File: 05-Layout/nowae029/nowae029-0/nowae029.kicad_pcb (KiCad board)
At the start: 2 copper layers, 100 x 99.9 mm, 144 parts, among them P101 COMM_3, P102 SUPPLY_3, P103 COMM_4, P104 SUPPLY_4, P201 DEBUG, P401 BATTERY, P501 632722110112, U201 STM32L073CBT6, U301 TCA9554PWR, U302 TCA9554PWR, U401 TLV70233DBV, U501 FT230XS, U601 TCA9554PWR, U602 TCA9554PWR, Y201 32768

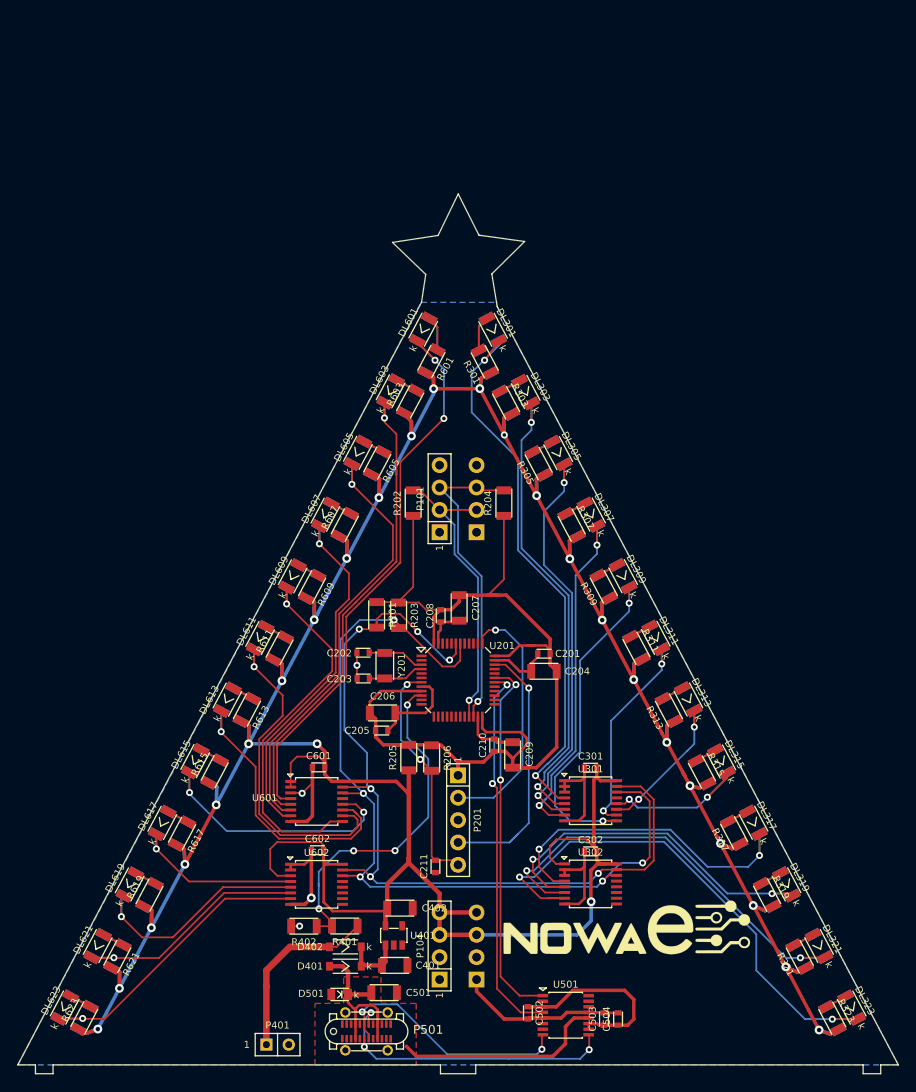
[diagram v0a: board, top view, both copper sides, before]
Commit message: WiP PCB TODO: resistors value into star page
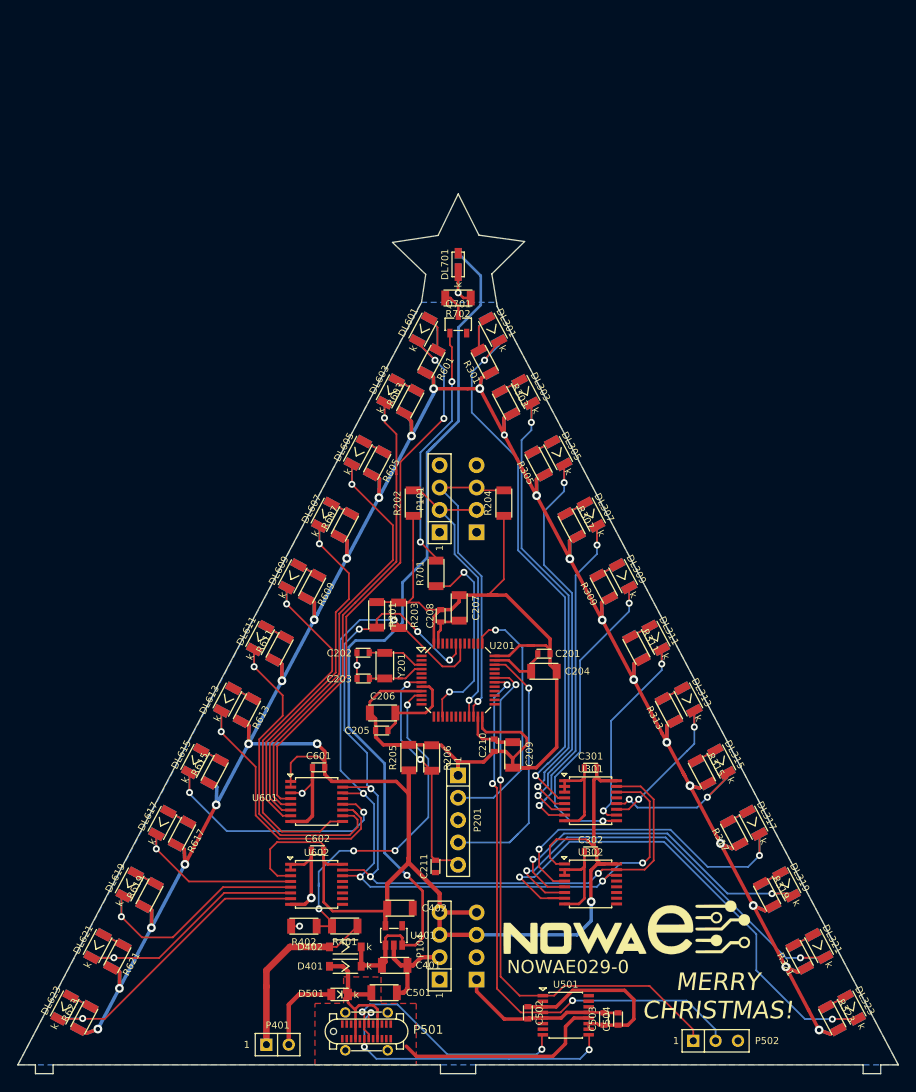
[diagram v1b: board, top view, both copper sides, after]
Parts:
- added DL701: WHITE, LEDs:LED-WURTH-WL_SWTP_3014, F.Cu at (100.0, 58.1)
- added DL702: WHITE, LEDs:LED-WURTH-WL_SWTP_3014, B.Cu at (100.0, 58.1)
- added P502: UART, CONNECTOR:CONN-STRIP-3x1-2.54, F.Cu at (129.2, 146.3)
- added Q701: BCW68GLT1G, SOT:SOT23-3, F.Cu at (100.0, 64.9)
- added R701: RESISTOR, RESISTOR:RESISTOR-1206, F.Cu at (97.5, 93.2)
- added R702: RESISTOR, RESISTOR:RESISTOR-1206, F.Cu at (100.0, 61.9)
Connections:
- net Net-(C401-Pad1) renamed +VDD
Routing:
- net +VDD: track 7.06 -> 104.9 mm, vias 0 -> 1
- net Net-(Q701-Pad1): track 0.00 -> 28.2 mm, vias 0 -> 2
- net /Microcontroller/STAR: track 0.00 -> 23.1 mm, vias 0 -> 2
- net /Communication/COMM_RX: track 43.8 -> 66.6 mm, vias 2 -> 3
- net GND: track 98.4 -> 119.7 mm
- net /Communication/COMM_TX: track 42.3 -> 63.2 mm
- net Net-(DL701-Pad1): track 0.00 -> 6.36 mm, vias 0 -> 1
- net Net-(Q701-Pad3): track 0.00 -> 2.94 mm
- net /Microcontroller/VDD_MCU: track 119.8 -> 120.4 mm
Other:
- board text added: "MERRY CHRISTMAS!"
- board text added: "NOWAE029-0"

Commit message: WiP: GND connections
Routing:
- net GND: track 119.7 -> 142.5 mm, vias 4 -> 13
- net +VDD: track 104.9 -> 101.9 mm
- net +VUSB: track 44.4 -> 47.0 mm
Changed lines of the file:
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@@
     (thickness 1.6)
     (drawings 57)
-    (tracks 1089)
+    (tracks 1128)
     (zones 0)
     (modules 150)
@@
   )
   (setup
-    (last_trace_width 0.2)
+    (last_trace_width 0.3)
     (user_trace_width 0.2)
     (user_trace_width 0.3)
@@
   (segment (start 108.3 104.3) (end 107.95 104.3) (width 0.3) (layer F.Cu) (net 2))
   (segment (start 105.75 103.05) (end 104.15 103.05) (width 0.3) (layer F.Cu) (net 2))
-  (segment (start 107 104.3) (end 105.75 103.05) (width 0.3) (layer F.Cu) (net 2))
   (segment (start 108.3 104.3) (end 108.3 103.41) (width 0.3) (layer F.Cu) (net 2))
   (segment (start 109.05 102.66) (end 109.05 102.3) (width 0.3) (layer F.Cu) (net 2))
-  (segment (start 108.3 103.41) (end 109.05 102.66) (width 0.3) (layer F.Cu) (net 2))
   (segment (start 99.97 98.7) (end 100.12 98.55) (width 0.3) (layer F.Cu) (net 2))
-  (segment (start 98.02 98.7) (end 99.97 98.7) (width 0.3) (layer F.Cu) (net 2))
   (segment (start 97.87 98.85) (end 98.02 98.7) (width 0.3) (layer F.Cu) (net 2))
   (segment (start 97.75 101.15) (end 97.75 99.88) (width 0.3) (layer F.Cu) (net 2))
@@
   (segment (start 96.314998 109.03) (end 92.88 109.03) (width 0.3) (layer F.Cu) (net 2))
   (segment (start 96.725 106.05) (end 97.09 106.415) (width 0.3) (layer F.Cu) (net 2))
-  (segment (start 97.09 106.415) (end 97.09 108.254998) (width 0.3) (layer F.Cu) (net 2))
   (segment (start 95.85 106.05) (end 96.725 106.05) (width 0.3) (layer F.Cu) (net 2))
   (segment (start 107 104.3) (end 108.3 104.3) (width 0.3) (layer F.Cu) (net 2))
@@
   (segment (start 95.818 136.77) (end 97.9 136.77) (width 0.5) (layer F.Cu) (net 2))
   (segment (start 94.888 137.7) (end 95.818 136.77) (width 0.5) (layer F.Cu) (net 2))
-  (segment (start 94.25 137.7) (end 94.25 140.37) (width 0.5) (layer F.Cu) (net 2))
   (segment (start 93.82 140.8) (end 93.05 140.8) (width 0.5) (layer F.Cu) (net 2))
   (segment (start 94.25 140.37) (end 93.82 140.8) (width 0.5) (layer F.Cu) (net 2))
@@
   (segment (start 80.77 142.166) (end 80.77 146.7) (width 0.5) (layer F.Cu) (net 2))
   (segment (start 81.936 141) (end 80.77 142.166) (width 0.5) (layer F.Cu) (net 2))
+  (segment (start 86.85 143.4) (end 87.2 143.05) (width 0.3) (layer F.Cu) (net 2))
+  (segment (start 86.85 144.37) (end 86.85 143.4) (width 0.3) (layer F.Cu) (net 2))
+  (segment (start 86.85 147) (end 87.2 147.35) (width 0.3) (layer F.Cu) (net 2))
+  (segment (start 86.85 146.03) (end 86.85 147) (width 0.3) (layer F.Cu) (net 2))
+  (segment (start 92.35 147) (end 92 147.35) (width 0.3) (layer F.Cu) (net 2))
+  (segment (start 92.35 146.03) (end 92.35 147) (width 0.3) (layer F.Cu) (net 2))
+  (segment (start 92.35 143.4) (end 92 143.05) (width 0.3) (layer F.Cu) (net 2))
+  (segment (start 92.35 144.37) (end 92.35 143.4) (width 0.3) (layer F.Cu) (net 2))
+  (via (at 94.25 139.35) (size 1) (drill 0.5) (layers F.Cu B.Cu) (net 2))
+  (segment (start 94.25 137.7) (end 94.25 139.35) (width 0.5) (layer F.Cu) (net 2))
+  (segment (start 94.25 139.35) (end 94.25 140.37) (width 0.5) (layer F.Cu) (net 2))
+  (segment (start 92.35 144.37) (end 92.35 146.03) (width 0.3) (layer F.Cu) (net 2))
+  (segment (start 86.85 144.37) (end 86.85 146.03) (width 0.3) (layer F.Cu) (net 2))
+  (segment (start 97.43 127.16) (end 96.88 127.16) (width 0.2) (layer F.Cu) (net 2))
+  (via (at 96.04 124.61) (size 0.8) (drill 0.4) (layers F.Cu B.Cu) (net 2))
+  (segment (start 96.04 126.32) (end 96.04 124.61) (width 0.2) (layer F.Cu) (net 2))
+  (segment (start 96.88 127.16) (end 96.04 126.32) (width 0.2) (layer F.Cu) (net 2))
+  (segment (start 94.85 135.802) (end 95.818 136.77) (width 0.4) (layer F.Cu) (net 2))
+  (segment (start 94.85 131.2) (end 94.85 135.802) (width 0.4) (layer F.Cu) (net 2))
+  (via (at 97.1 107.13) (size 0.8) (drill 0.4) (layers F.Cu B.Cu) (net 2))
+  (segment (start 97.09 107.12) (end 97.1 107.13) (width 0.4) (layer F.Cu) (net 2))
+  (segment (start 97.09 106.415) (end 97.09 107.12) (width 0.3) (layer F.Cu) (net 2))
+  (segment (start 97.09 107.12) (end 97.09 108.254998) (width 0.3) (layer F.Cu) (net 2))
+  (via (at 102.25 111.51) (size 0.8) (drill 0.4) (layers F.Cu B.Cu) (net 2))
+  (segment (start 107 104.3) (end 105.75 103.05) (width 0.3) (layer F.Cu) (net 2))
+  (segment (start 108.645 103.065) (end 108.64 103.06) (width 0.4) (layer F.Cu) (net 2))
+  (via (at 108.64 103.06) (size 0.8) (drill 0.4) (layers F.Cu B.Cu) (net 2))
+  (segment (start 108.3 103.41) (end 108.645 103.065) (width 0.3) (layer F.Cu) (net 2))
+  (segment (start 108.645 103.065) (end 109.05 102.66) (width 0.3) (layer F.Cu) (net 2))
+  (via (at 98.83 98.68) (size 0.8) (drill 0.4) (layers F.Cu B.Cu) (net 2))
+  (segment (start 98.81 98.7) (end 98.83 98.68) (width 0.4) (layer F.Cu) (net 2))
+  (segment (start 98.02 98.7) (end 98.81 98.7) (width 0.3) (layer F.Cu) (net 2))
+  (segment (start 98.81 98.7) (end 99.97 98.7) (width 0.3) (layer F.Cu) (net 2))
+  (via (at 110.94 121.325) (size 0.8) (drill 0.4) (layers F.Cu B.Cu) (net 2))
+  (segment (start 110.99 121.275) (end 110.94 121.325) (width 0.3) (layer F.Cu) (net 2))
+  (segment (start 112.1 121.275) (end 110.99 121.275) (width 0.3) (layer F.Cu) (net 2))
+  (via (at 110.48 130.775) (size 0.8) (drill 0.4) (layers F.Cu B.Cu) (net 2))
+  (segment (start 110.53 130.725) (end 110.48 130.775) (width 0.3) (layer F.Cu) (net 2))
+  (segment (start 112.1 130.725) (end 110.53 130.725) (width 0.3) (layer F.Cu) (net 2))
+  (via (at 100.97 67.15) (size 0.8) (drill 0.4) (layers F.Cu B.Cu) (net 2))
+  (segment (start 100.97 65.89) (end 100.97 67.15) (width 0.3) (layer F.Cu) (net 2))
   (segment (start 91.66 102.19) (end 91.68 102.21) (width 0.2) (layer F.Cu) (net 3))
   (segment (start 89.91 102.19) (end 91.66 102.19) (width 0.2) (layer F.Cu) (net 3))
@@
   (segment (start 112.2 144.65) (end 112.2 146.59) (width 0.4) (layer F.Cu) (net 7))
   (segment (start 95.270001 148.030001) (end 94.12 146.88) (width 0.4) (layer F.Cu) (net 7))
+  (segment (start 88.35 146.03) (end 88.35 147.278) (width 0.3) (layer F.Cu) (net 7))
+  (segment (start 90.85 146.03) (end 90.85 147.072) (width 0.3) (layer F.Cu) (net 7))
+  (segment (start 90.85 147.072) (end 90.64 147.282) (width 0.3) (layer F.Cu) (net 7))
   (segment (start 114.83 144.9475) (end 114.83 144.3125) (width 0.3) (layer F.Cu) (net 8))
   (segment (start 114.83 144.3125) (end 115.8025 144.3125) (width 0.3) (layer F.Cu) (net 8))
@@
   (segment (start 97.371 78.575) (end 96.736 79.21) (width 0.3) (layer B.Cu) (net 152))
   (via (at 94.196 127.47) (size 0.8) (drill 0.4) (layers F.Cu B.Cu) (net 152))
-  (segment (start 94.196 127.47) (end 95.974 129.248) (width 0.3) (layer F.Cu) (net 152))
-  (segment (start 95.974 129.248) (end 95.974 134.582) (width 0.3) (layer F.Cu) (net 152))
-  (segment (start 95.156 135.4) (end 93.65 135.4) (width 0.3) (layer F.Cu) (net 152))
-  (segment (start 95.974 134.582) (end 95.156 135.4) (width 0.3) (layer F.Cu) (net 152))
-  (segment (start 91.75 134.57) (end 91.992 134.328) (width 0.3) (layer F.Cu) (net 152))
-  (segment (start 91.75 135.4) (end 91.75 134.57) (width 0.3) (layer F.Cu) (net 152))
-  (segment (start 91.992 134.328) (end 93.434 134.328) (width 0.3) (layer F.Cu) (net 152))
-  (segment (start 93.434 134.328) (end 93.688 134.582) (width 0.3) (layer F.Cu) (net 152))
-  (segment (start 93.65 134.62) (end 93.65 135.4) (width 0.3) (layer F.Cu) (net 152))
-  (segment (start 93.688 134.582) (end 93.65 134.62) (width 0.3) (layer F.Cu) (net 152))
   (segment (start 102.578 59.378) (end 100.02 56.82) (width 0.3) (layer B.Cu) (net 152))
   (segment (start 102.578 62.7) (end 102.578 59.378) (width 0.3) (layer B.Cu) (net 152))
@@
   (segment (start 96.482 79.464) (end 96.482 91.402) (width 0.3) (layer B.Cu) (net 152))
   (segment (start 97.371 78.575) (end 96.482 79.464) (width 0.3) (layer B.Cu) (net 152))
+  (segment (start 91.75 134.57) (end 91.75 135.4) (width 0.3) (layer F.Cu) (net 152))
+  (segment (start 91.992 134.328) (end 91.75 134.57) (width 0.3) (layer F.Cu) (net 152))
+  (segment (start 93.65 134.544) (end 93.434 134.328) (width 0.3) (layer F.Cu) (net 152))
+  (segment (start 93.65 135.4) (end 93.65 134.544) (width 0.3) (layer F.Cu) (net 152))
+  (segment (start 94.196 127.47) (end 94.196 128.954) (width 0.3) (layer F.Cu) (net 152))
+  (segment (start 94.196 128.954) (end 92.85 130.3) (width 0.3) (layer F.Cu) (net 152))
+  (segment (start 92.85 130.3) (end 92.85 133.97) (width 0.3) (layer F.Cu) (net 152))
+  (segment (start 92.492 134.328) (end 91.992 134.328) (width 0.3) (layer F.Cu) (net 152))
+  (segment (start 92.85 133.97) (end 92.492 134.328) (width 0.3) (layer F.Cu) (net 152))
+  (segment (start 93.434 134.328) (end 92.492 134.328) (width 0.3) (layer F.Cu) (net 152))
   (segment (start 100.01 58.97) (end 100.01 61.31) (width 0.3) (layer F.Cu) (net 153))
   (segment (start 100.6 61.9) (end 101.44 61.9) (width 0.3) (layer F.Cu) (net 153))

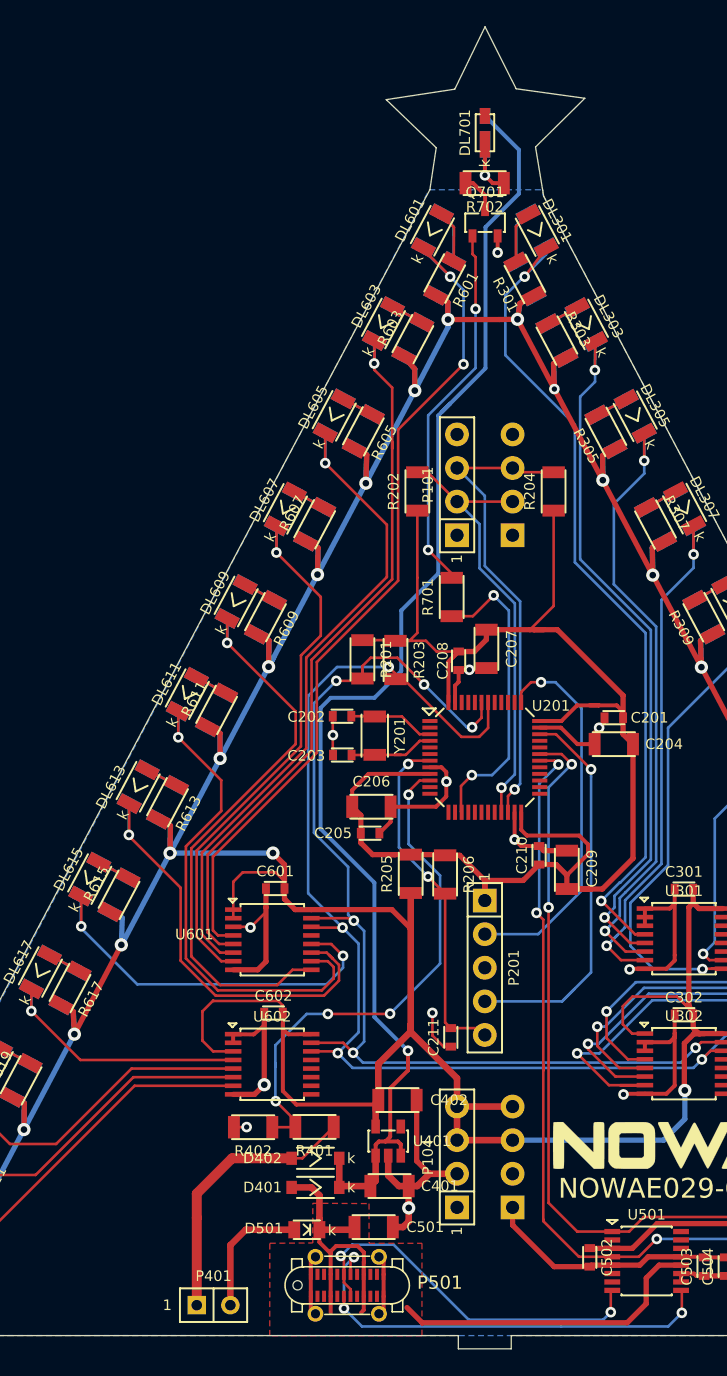
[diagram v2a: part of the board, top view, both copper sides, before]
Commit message: Added test point footprint. PCB route ended!
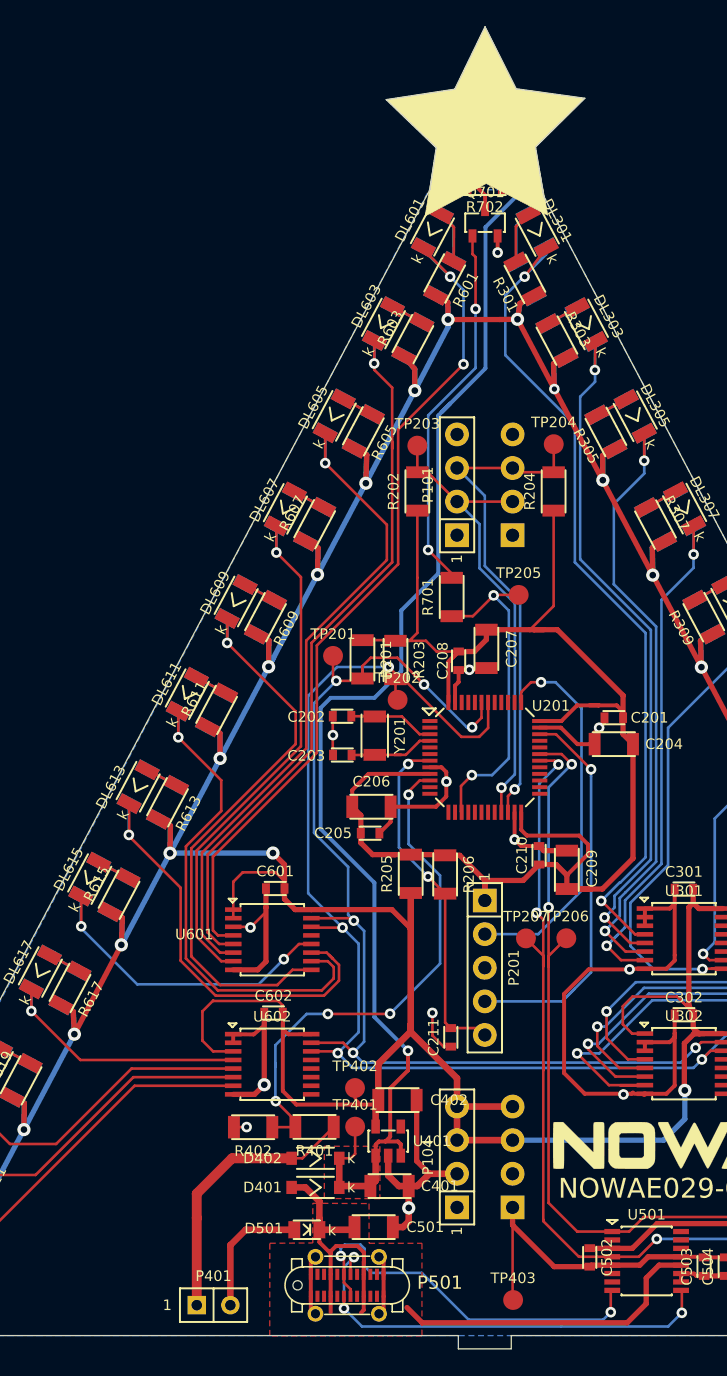
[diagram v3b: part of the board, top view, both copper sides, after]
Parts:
- added TP201: TEST_POINT, MISC:TESTPOINT-1.5MM-SMD, F.Cu at (88.5, 97.6)
- added TP202: TEST_POINT, MISC:TESTPOINT-1.5MM-SMD, F.Cu at (93.4, 101.0)
- added TP203: TEST_POINT, MISC:TESTPOINT-1.5MM-SMD, F.Cu at (94.9, 81.7)
- added TP204: TEST_POINT, MISC:TESTPOINT-1.5MM-SMD, F.Cu at (105.2, 81.6)
- added TP205: TEST_POINT, MISC:TESTPOINT-1.5MM-SMD, F.Cu at (102.6, 93.0)
- added TP206: TEST_POINT, MISC:TESTPOINT-1.5MM-SMD, F.Cu at (106.2, 119.0)
- added TP207: TEST_POINT, MISC:TESTPOINT-1.5MM-SMD, F.Cu at (103.1, 119.0)
- added TP401: TEST_POINT, MISC:TESTPOINT-1.5MM-SMD, F.Cu at (90.2, 133.2)
- added TP402: TEST_POINT, MISC:TESTPOINT-1.5MM-SMD, F.Cu at (90.2, 130.3)
- added TP403: TEST_POINT, MISC:TESTPOINT-1.5MM-SMD, F.Cu at (102.1, 146.3)
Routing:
- net GND: track 142.5 -> 166.3 mm
- net +VDD: track 101.9 -> 110.1 mm, vias 1 -> 2
- net /Branch2/B2_LINE8: track 30.5 -> 25.1 mm
- net +3.3V: track 447.5 -> 452.0 mm
- net /Communication/COMM_TX: track 63.2 -> 65.9 mm
- net /Communication/COMM_RX: track 66.6 -> 69.3 mm
- net /B_EXT_SCL: track 35.8 -> 37.9 mm
- net /B_EXT_SDA: track 33.8 -> 35.8 mm
- net /Branch1/BRANCH1_SDA: track 99.5 -> 101.5 mm
- net /Microcontroller/STAR: track 23.1 -> 25.0 mm
- net /Branch1/BRANCH1_SCL: track 99.9 -> 101.6 mm
- net /Branch2/B2_LINE4: track 41.9 -> 40.6 mm
- net Net-(P501-PadA6): track 28.4 -> 29.5 mm
- net +VUSB: track 47.0 -> 47.6 mm
- added copper zone on F.Cu, net +VDD
